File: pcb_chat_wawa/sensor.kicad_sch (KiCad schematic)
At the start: 6 parts, among them J1 Conn_01x08, J5 Conn_01x05, J6 Conn_01x05, U5 ADXL343

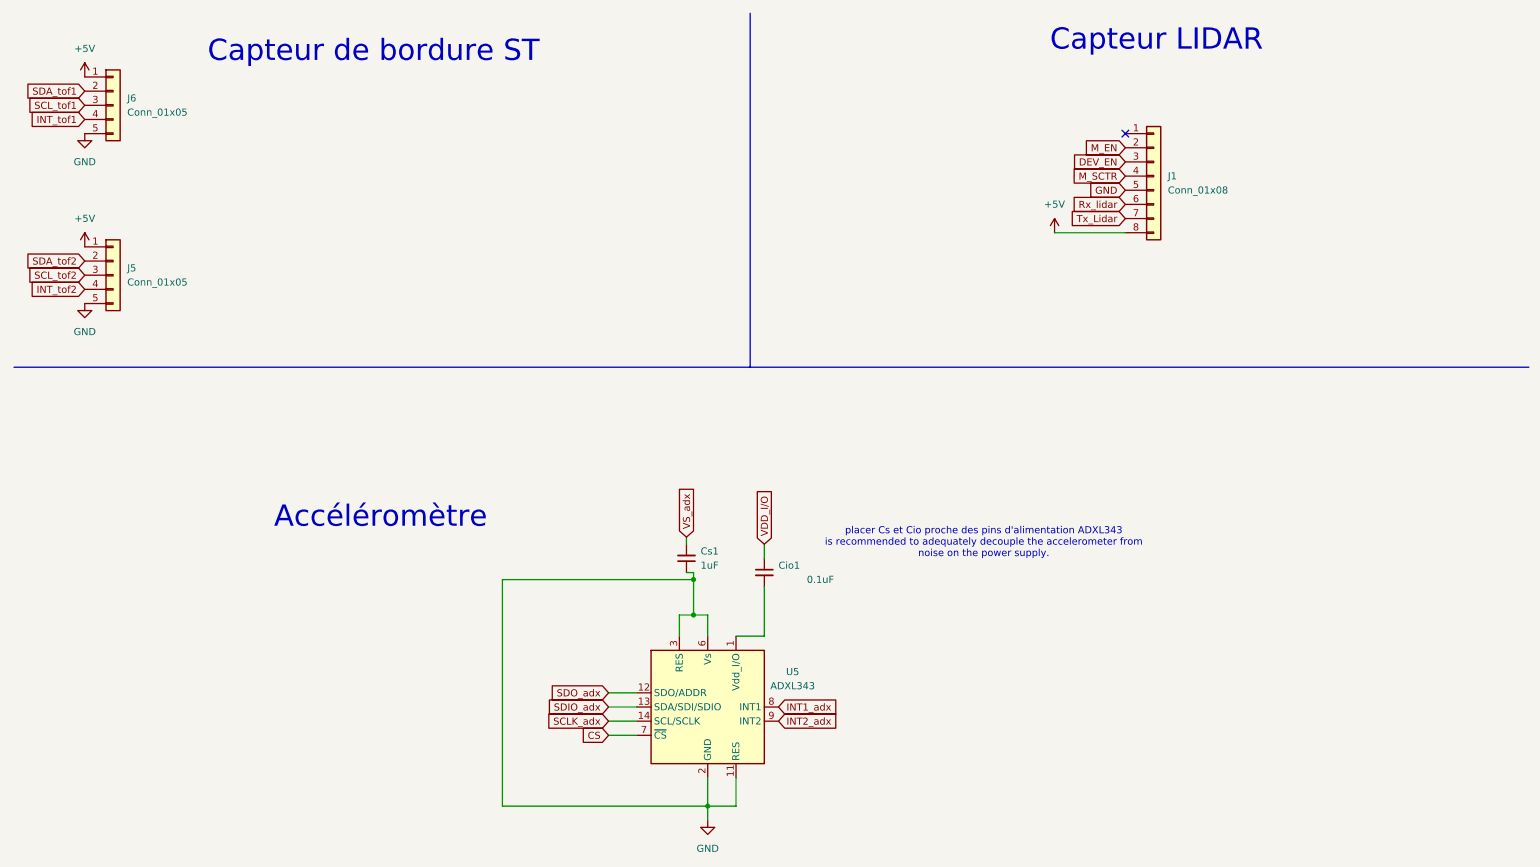
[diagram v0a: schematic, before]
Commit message: modification i2c labels+ajout R à dimmensionner
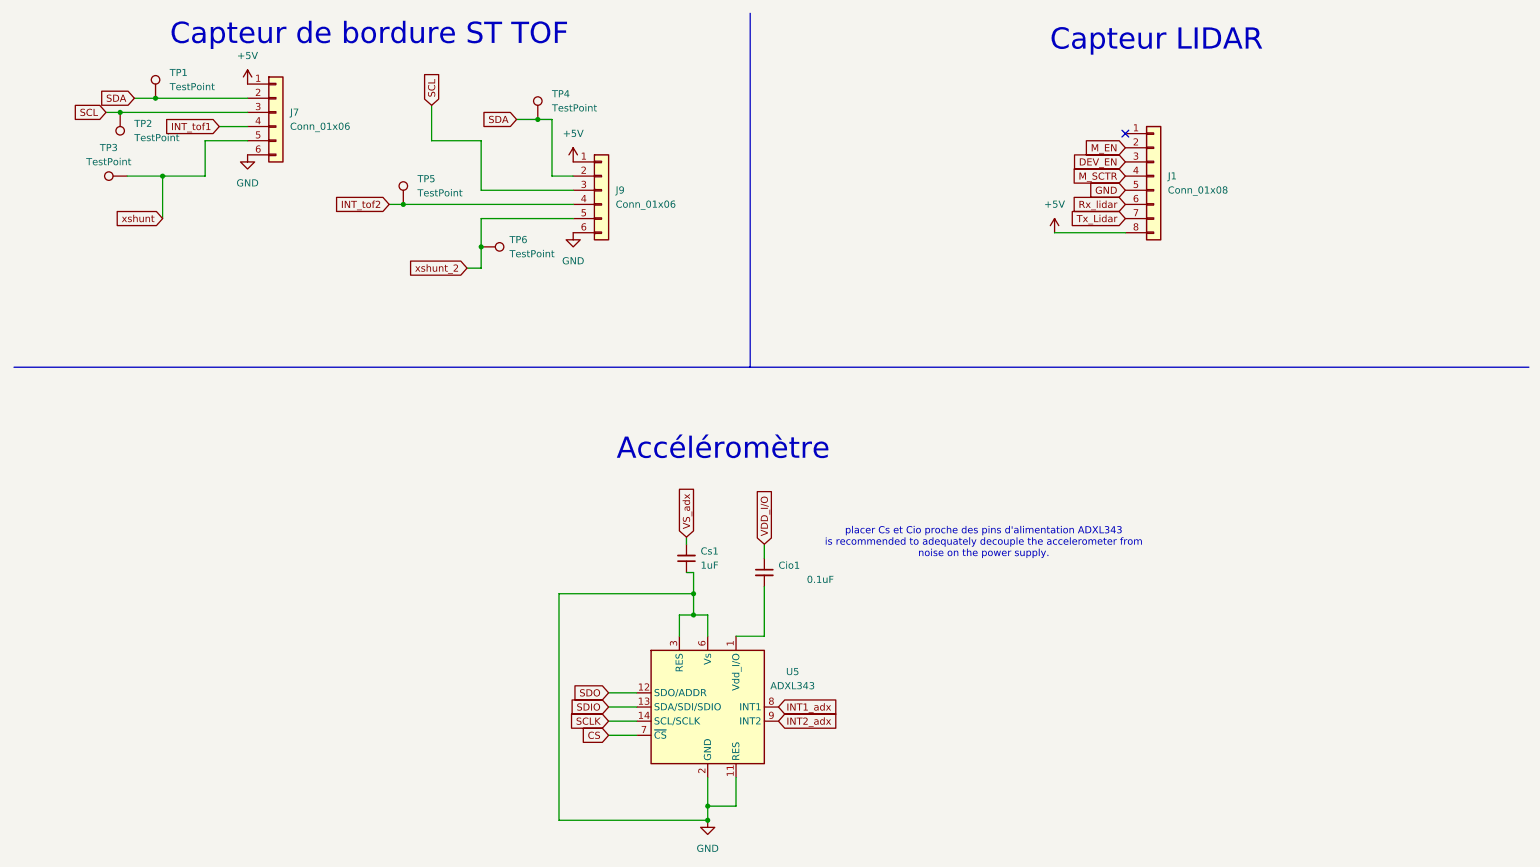
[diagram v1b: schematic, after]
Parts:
- removed J5, J6: Conn_01x05, Connector_JST:JST_XH_S8B-XH-A_1x08_P2.50mm_Horizontal, symbol Connector_Generic:Conn_01x05
- added J7, J9: Conn_01x06, symbol Connector_Generic:Conn_01x06
- added TP1, TP2, TP3, TP4, TP5, TP6: TestPoint, symbol Connector:TestPoint
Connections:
- net +5V: now also J7.1 (Pin_1), J9.1 (Pin_1)
- net GND: now also J7.6 (Pin_6), J9.6 (Pin_6)
- net INT_tof1: now also J7.4 (Pin_4)
- net INT_tof2: now also J9.4 (Pin_4), TP5.1
- net SCLK_adx renamed SCLK
- net SDIO_adx renamed SDIO
- net SDO_adx renamed SDO
- new net SCL: J7.3 (Pin_3), J9.3 (Pin_3), TP2.1
- new net SDA: J7.2 (Pin_2), J9.2 (Pin_2), TP1.1, TP4.1
- new net xshunt: J7.5 (Pin_5), TP3.1
- new net xshunt_2: J9.5 (Pin_5), TP6.1
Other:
- note added: "Capteur de bordure ST TOF"
- note removed: "Capteur de bordure ST"
